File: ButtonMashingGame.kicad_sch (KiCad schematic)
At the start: 59 parts, among them Q1 PNP, Q2 PNP, SW1 RESET, SW2 P1, SW3 P2, U1 74LS393, U2 74LS193, U3 74LS04, U4 CD4051B, U5 74LS74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

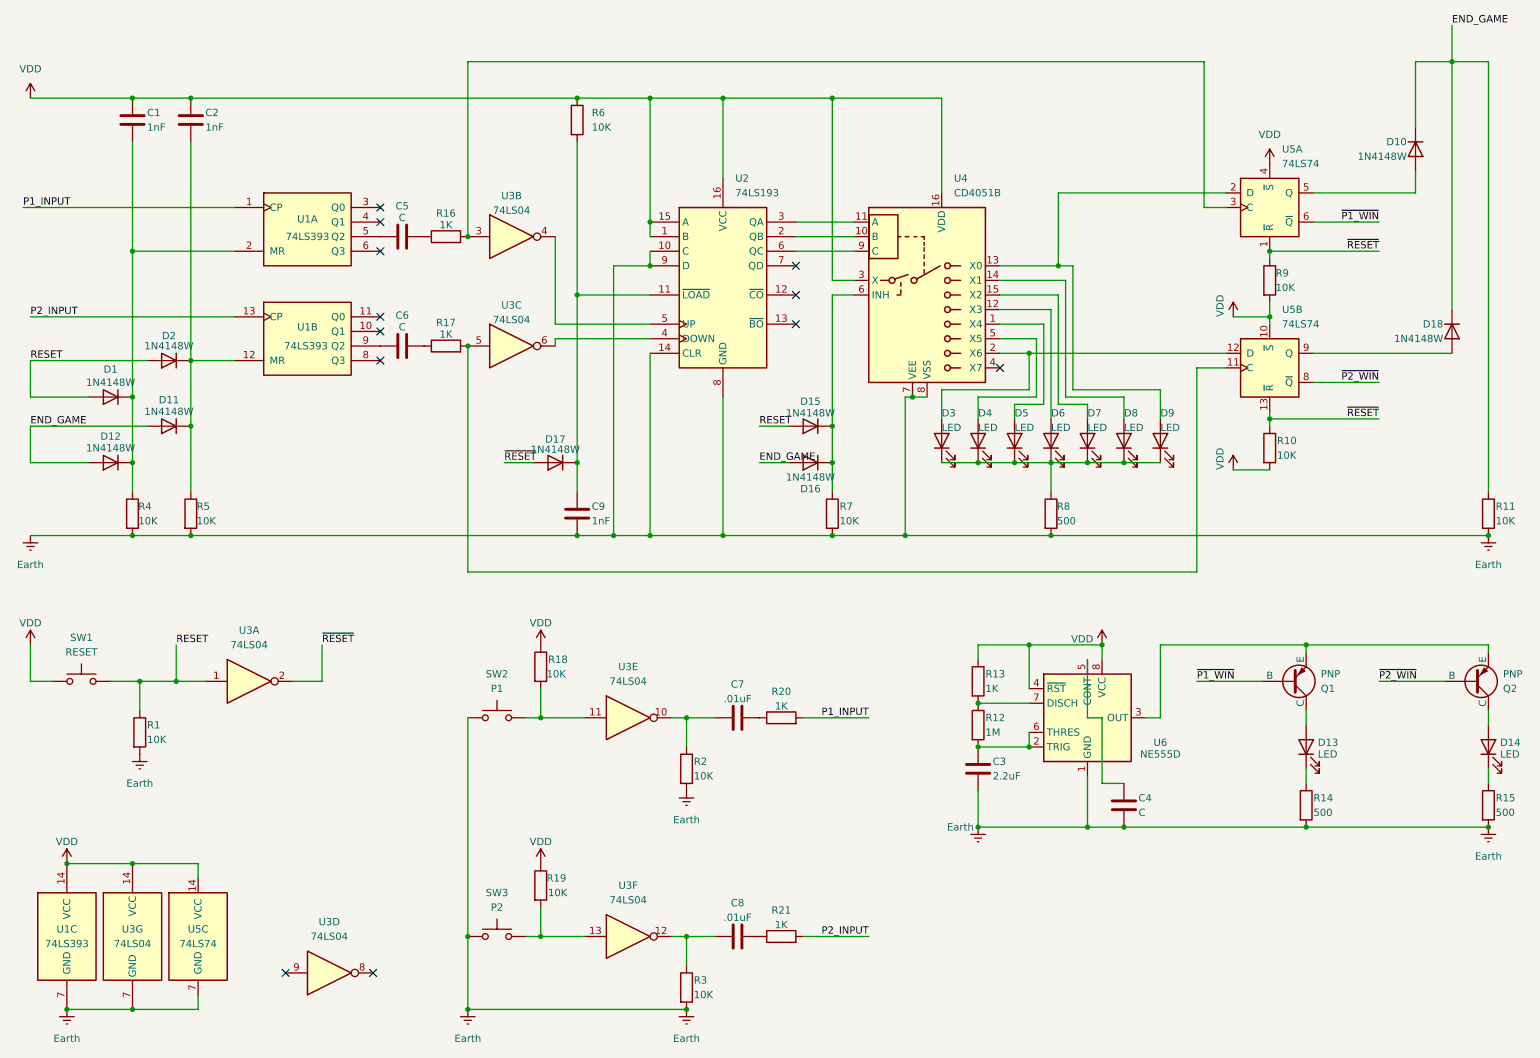
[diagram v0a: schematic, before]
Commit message: Replaced 04 inverter with schmitt triggered 14 inverters
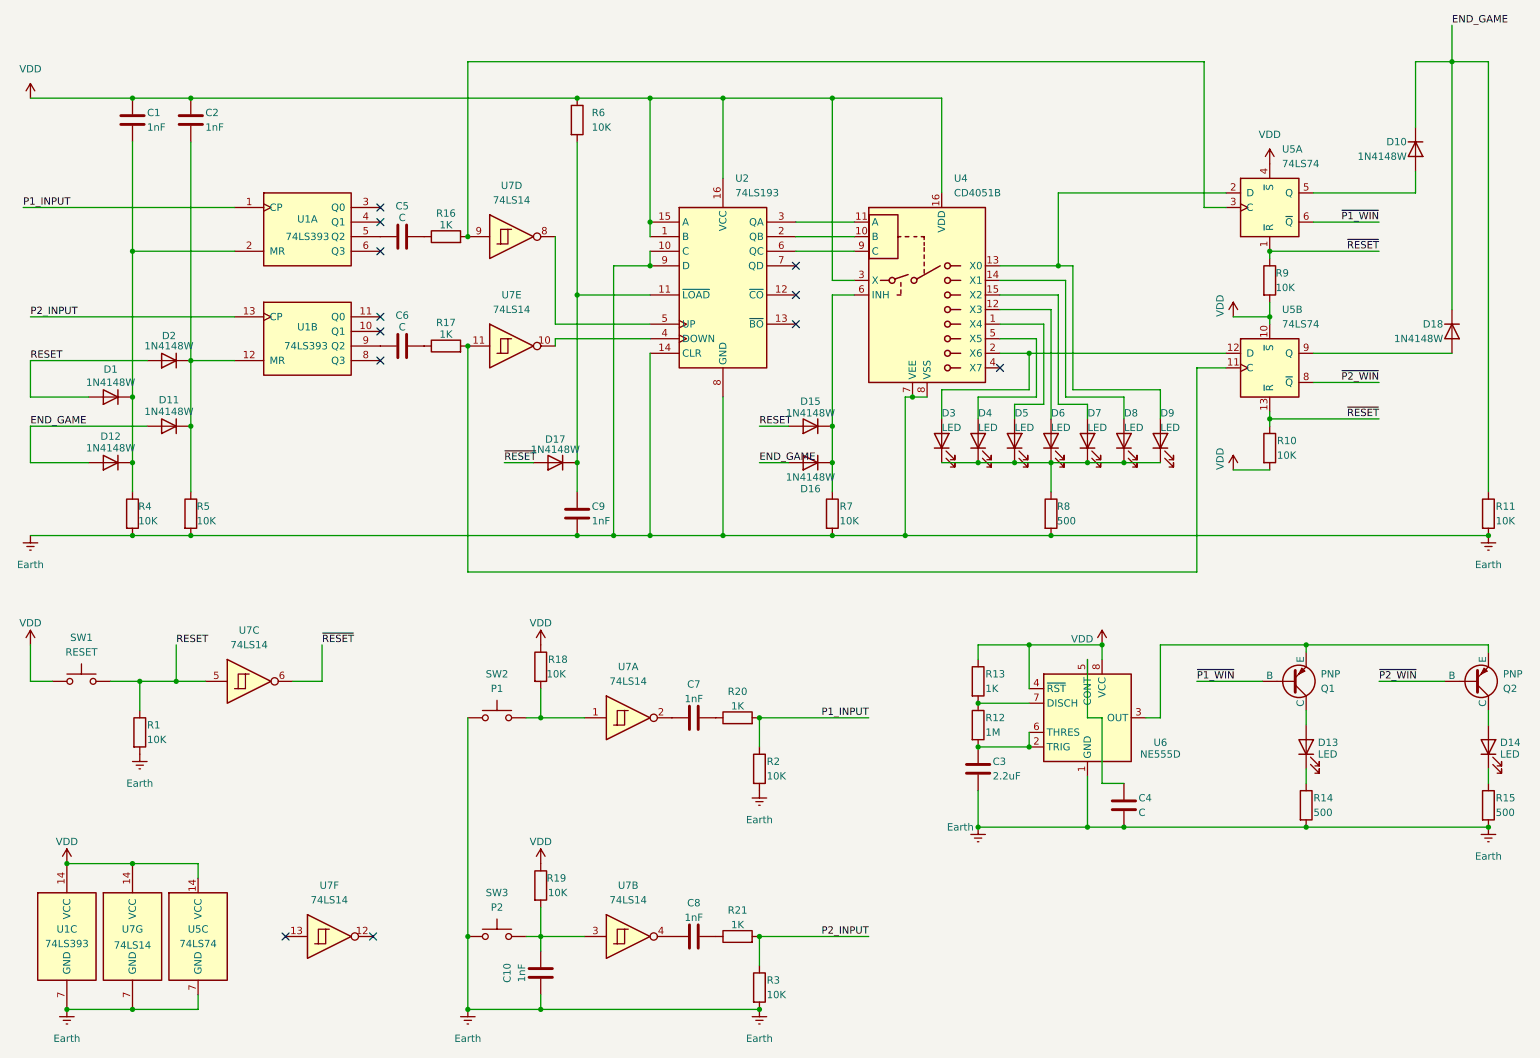
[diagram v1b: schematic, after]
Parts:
- removed U3: 74LS04, symbol 74xx:74LS04
- added C10: 1nF, symbol Device:C
- added U7: 74LS14, symbol 74xx:74LS14
- C7, C8: value .01uF -> 1nF
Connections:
- net Earth: now also C10.1, U7.7 (GND)
- net P1_INPUT: now also R2.1
- net P2_INPUT: now also R3.1
- net RESET: now also U7.5
- net VDD: now also U7.14 (VCC)
- net ~{RESET}: now also U7.6
- net at C8.1: now also U7.4; no longer R3.1
- net at C7.1: now also U7.2; no longer R2.1
- net at R18.2, SW2.2: now also U7.1
- net at R16.2, U5.3 (C): now also U7.9
- net at U2.5 (UP): now also U7.8
- net at R19.2, SW3.2: now also C10.2, U7.3
- net at R17.2, U5.11 (C): now also U7.11
- net at U2.4 (DOWN): now also U7.10
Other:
- moved on the sheet: C7, C8, R2, R20, R21, R3
